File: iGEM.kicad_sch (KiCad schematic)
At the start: 50 parts, among them IC1 TMCS1107A1BQDRQ1, IC2 TMCS1107A1BQDRQ1, IC3 MCP4642-502E_UN, J1 Conn_01x02, J2 Conn_01x02, J3 Conn_01x02, J4 Conn_01x03, M1 Fan, Q1 TIP122, Q2 TIP122, Q3 IRF4905, Q4 D44VH, Q5 IRF4905, Q6 D44VH, U1 ADC101C021CIMK, U2 ADC101C021CIMK, U3 PCA9536D, U4 ICL7667

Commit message: updated mounting holes to M3
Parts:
- H1, H2, H3, H4: footprint MountingHole:MountingHole_5.3mm_M5_DIN965_Pad -> MountingHole:MountingHole_3.2mm_M3_DIN965_Pad
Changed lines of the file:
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@@
       (effects (font (size 1.27 1.27)) (justify left))
     )
-    (property "Footprint" "MountingHole:MountingHole_5.3mm_M5_DIN965_Pad" (id 2) (at 243.84 22.225 0)
+    (property "Footprint" "MountingHole:MountingHole_3.2mm_M3_DIN965_Pad" (id 2) (at 243.84 22.225 0)
       (effects (font (size 1.27 1.27)) hide)
     )
@@
       (effects (font (size 1.27 1.27)) (justify left))
     )
-    (property "Footprint" "MountingHole:MountingHole_5.3mm_M5_DIN965_Pad" (id 2) (at 228.727 22.098 0)
+    (property "Footprint" "MountingHole:MountingHole_3.2mm_M3_DIN965_Pad" (id 2) (at 228.727 22.098 0)
       (effects (font (size 1.27 1.27)) hide)
     )
@@
       (effects (font (size 1.27 1.27)) (justify left))
     )
-    (property "Footprint" "MountingHole:MountingHole_5.3mm_M5_DIN965_Pad" (id 2) (at 236.093 22.098 0)
+    (property "Footprint" "MountingHole:MountingHole_3.2mm_M3_DIN965_Pad" (id 2) (at 236.093 22.098 0)
       (effects (font (size 1.27 1.27)) hide)
     )
@@
       (effects (font (size 1.27 1.27)) (justify left))
     )
-    (property "Footprint" "MountingHole:MountingHole_5.3mm_M5_DIN965_Pad" (id 2) (at 220.98 21.971 0)
+    (property "Footprint" "MountingHole:MountingHole_3.2mm_M3_DIN965_Pad" (id 2) (at 220.98 21.971 0)
       (effects (font (size 1.27 1.27)) hide)
     )
@@
     )
     (path "/d8a1e4a6-2d49-424a-897c-8468ef6206d3"
-      (reference "H1") (unit 1) (value "MH") (footprint "MountingHole:MountingHole_5.3mm_M5_DIN965_Pad")
+      (reference "H1") (unit 1) (value "MH") (footprint "MountingHole:MountingHole_3.2mm_M3_DIN965_Pad")
     )
     (path "/a74e7590-46b6-4ec0-8175-bac4032efc02"
-      (reference "H2") (unit 1) (value "MH") (footprint "MountingHole:MountingHole_5.3mm_M5_DIN965_Pad")
+      (reference "H2") (unit 1) (value "MH") (footprint "MountingHole:MountingHole_3.2mm_M3_DIN965_Pad")
     )
     (path "/d1b51eea-8e22-4d48-82b7-9ab39c45531f"
-      (reference "H3") (unit 1) (value "MH") (footprint "MountingHole:MountingHole_5.3mm_M5_DIN965_Pad")
+      (reference "H3") (unit 1) (value "MH") (footprint "MountingHole:MountingHole_3.2mm_M3_DIN965_Pad")
     )
     (path "/7d301b82-72a3-482a-8606-544009d9efa6"
-      (reference "H4") (unit 1) (value "MH") (footprint "MountingHole:MountingHole_5.3mm_M5_DIN965_Pad")
+      (reference "H4") (unit 1) (value "MH") (footprint "MountingHole:MountingHole_3.2mm_M3_DIN965_Pad")
     )
     (path "/51879485-f54c-4d64-8de1-5fd9b52a4051"

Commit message: increased current capacity and added useful silk
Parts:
- J4: footprint Connector_JST:JST_XH_B3B-XH-AM_1x03_P2.50mm_Vertical -> Connector_JST:JST_XH_B3B-XH-A_1x03_P2.50mm_Vertical
- M1: footprint Connector_JST:JST_XH_B2B-XH-AM_1x02_P2.50mm_Vertical -> Connector_JST:JST_XH_B2B-XH-A_1x02_P2.50mm_Vertical
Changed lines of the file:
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@@
       (effects (font (size 1.27 1.27)) (justify left))
     )
-    (property "Footprint" "Connector_JST:JST_XH_B3B-XH-AM_1x03_P2.50mm_Vertical" (id 2) (at 226.695 58.039 0)
+    (property "Footprint" "Connector_JST:JST_XH_B3B-XH-A_1x03_P2.50mm_Vertical" (id 2) (at 226.695 58.039 0)
       (effects (font (size 1.27 1.27)) hide)
     )
@@
       (effects (font (size 1.27 1.27)) (justify left))
     )
-    (property "Footprint" "Connector_JST:JST_XH_B2B-XH-AM_1x02_P2.50mm_Vertical" (id 2) (at 263.398 26.924 0)
+    (property "Footprint" "Connector_JST:JST_XH_B2B-XH-A_1x02_P2.50mm_Vertical" (id 2) (at 263.398 26.924 0)
       (effects (font (size 1.27 1.27)) hide)
     )
@@
     )
     (path "/c0df6d10-baa8-43f2-8eaf-37632beb3c98"
-      (reference "J4") (unit 1) (value "Conn_01x03") (footprint "Connector_JST:JST_XH_B3B-XH-AM_1x03_P2.50mm_Vertical")
+      (reference "J4") (unit 1) (value "Conn_01x03") (footprint "Connector_JST:JST_XH_B3B-XH-A_1x03_P2.50mm_Vertical")
     )
     (path "/d65d8be2-cc90-4c64-af7a-fe7ceb3f9386"
-      (reference "M1") (unit 1) (value "Fan") (footprint "Connector_JST:JST_XH_B2B-XH-AM_1x02_P2.50mm_Vertical")
+      (reference "M1") (unit 1) (value "Fan") (footprint "Connector_JST:JST_XH_B2B-XH-A_1x02_P2.50mm_Vertical")
     )
     (path "/4b59aaf5-2612-4b64-b615-ddf78dad43ca"

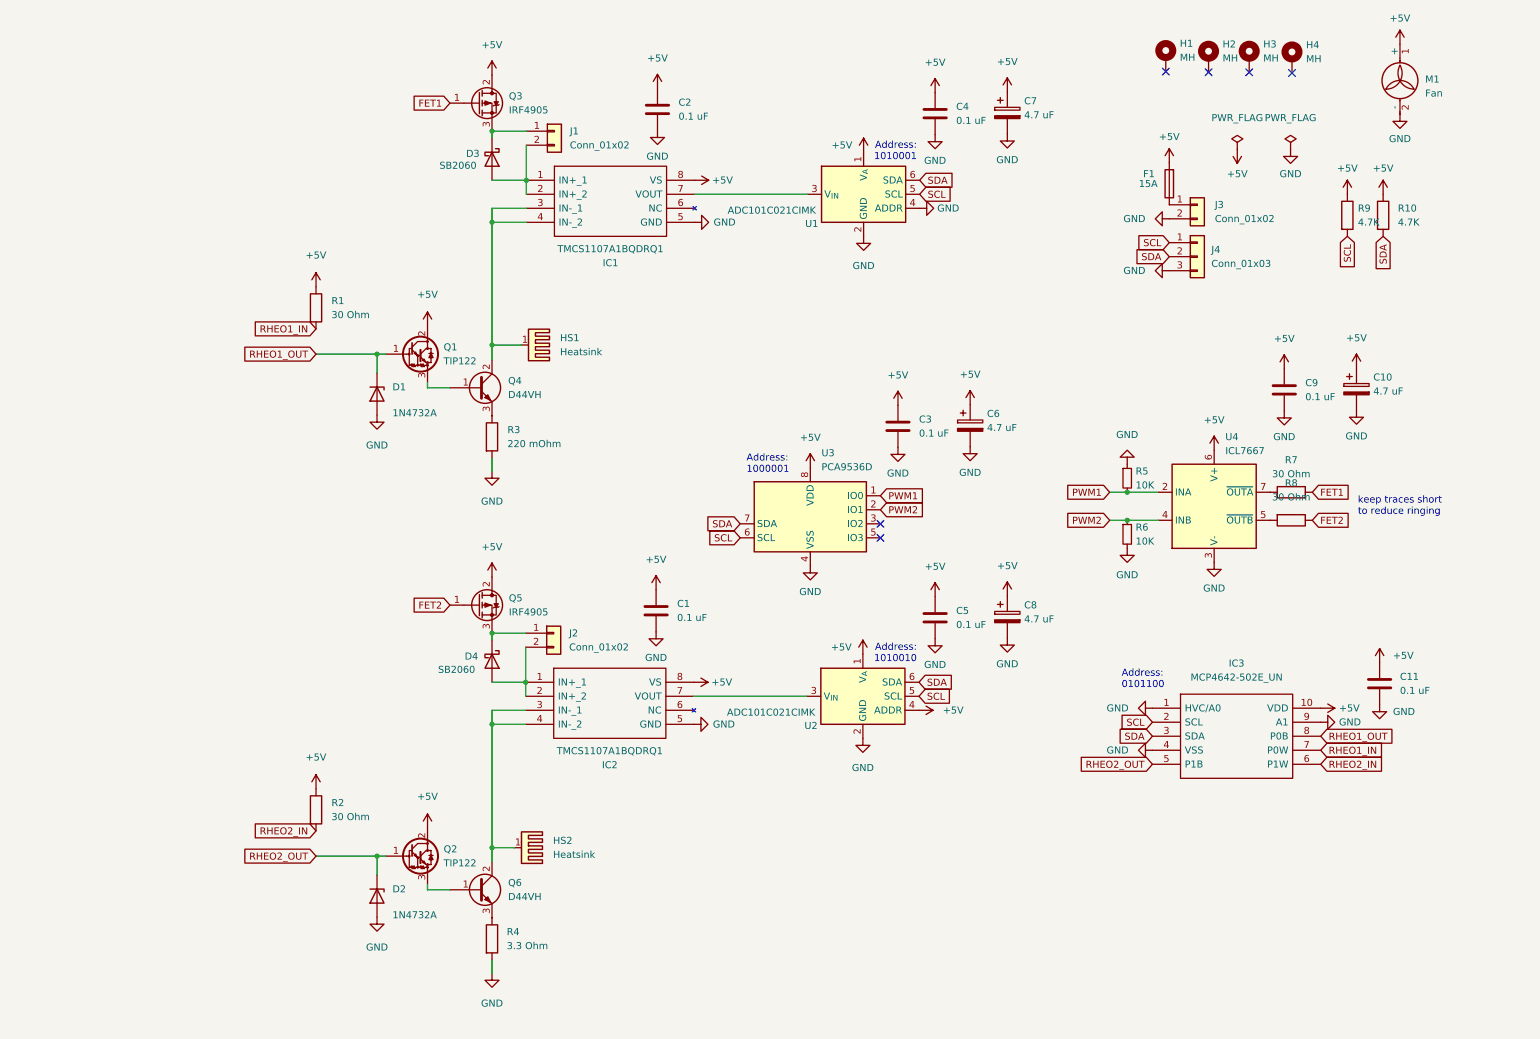
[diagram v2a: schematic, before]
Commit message: Changed to a single H-bridge for a single coil. Many parts changes. Addresses now configurable via pin header
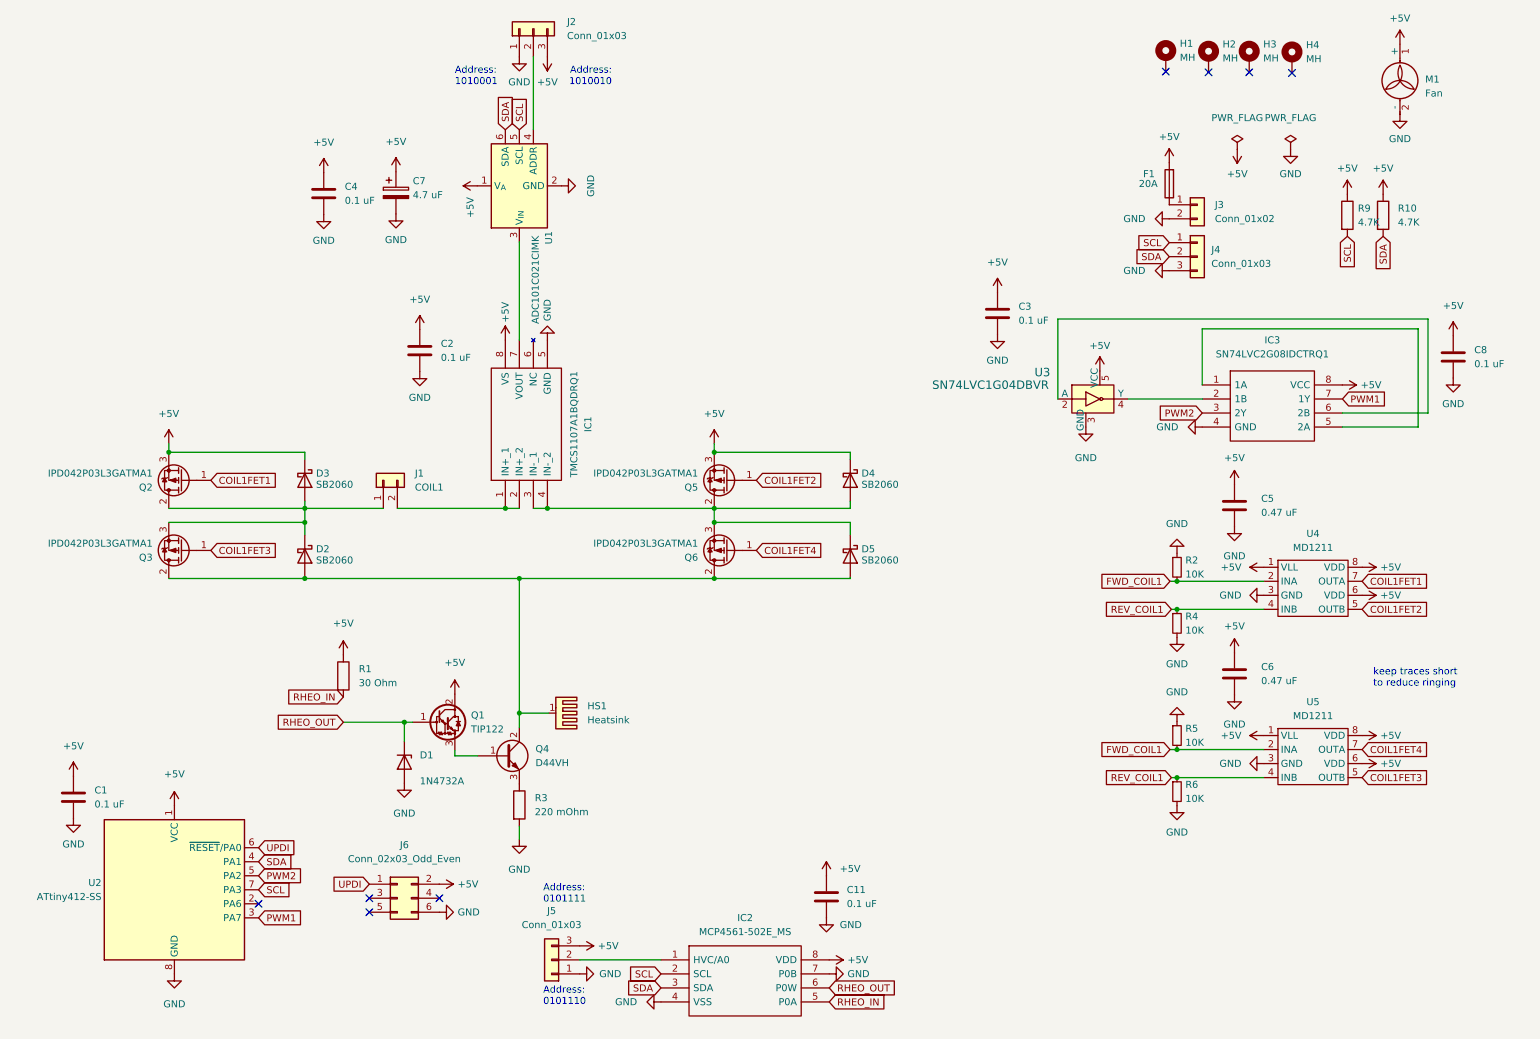
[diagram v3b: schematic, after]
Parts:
- removed C10, C6, C8: 4.7 uF, Capacitor_Tantalum_SMD:CP_EIA-3528-21_Kemet-B_Pad1.50x2.35mm_HandSolder, symbol Device:C_Polarized
- removed C9: 0.1 uF, Capacitor_SMD:C_0805_2012Metric_Pad1.18x1.45mm_HandSolder, symbol Device:C
- removed D2: 1N4732A, Diode_THT:D_DO-41_SOD81_P10.16mm_Horizontal, symbol Diode:1N47xxA
- removed HS2: Heatsink, Heatsink:Heatsink_AAVID_576802B03900G, symbol Mechanical:Heatsink_Pad
- removed IC2: TMCS1107A1BQDRQ1, Package_SO:SOIC-8_3.9x4.9mm_P1.27mm, symbol TMCS1107A1BQDRQ1:TMCS1107A1BQDRQ1
- removed IC3: MCP4642-502E_UN, Package_SO:MSOP-10_3x3mm_P0.5mm, symbol MCP4642-502E_UN:MCP4642-502E_UN
- removed J2: Conn_01x02, TerminalBlock:TerminalBlock_bornier-2_P5.08mm, symbol Connector_Generic:Conn_01x02
- removed Q2: TIP122, Package_TO_SOT_THT:TO-220-3_Vertical, symbol Transistor_BJT:TIP122
- removed Q3, Q5: IRF4905, Package_TO_SOT_THT:TO-220-3_Vertical, symbol Transistor_FET:IRF4905
- removed Q6: D44VH, Package_TO_SOT_THT:TO-220-3_Vertical, symbol Device:Q_NPN_BCE
- removed R2, R7, R8: 30 Ohm, Capacitor_SMD:C_0805_2012Metric_Pad1.18x1.45mm_HandSolder, symbol Device:R
- removed R4: 3.3 Ohm, TerminalBlock:TerminalBlock_bornier-2_P5.08mm, symbol Device:R
- removed U2: ADC101C021CIMK, Package_TO_SOT_SMD:SOT-23-6, symbol Analog_ADC:ADC101C021CIMK
- removed U3: PCA9536D, Package_SO:SOIC-8_3.9x4.9mm_P1.27mm, symbol Interface_Expansion:PCA9536D
- removed U4: ICL7667, Package_SO:SOIC-8_3.9x4.9mm_P1.27mm, symbol Driver_FET:ICL7667
- added C6: 0.47 uF, Capacitor_SMD:C_0805_2012Metric_Pad1.18x1.45mm_HandSolder, symbol Device:C
- added C8: 0.1 uF, Capacitor_SMD:C_0805_2012Metric_Pad1.18x1.45mm_HandSolder, symbol Device:C
- added D2, D5: SB2060, Diode_THT:D_DO-201AD_P12.70mm_Horizontal, symbol Device:D_Schottky
- added IC2: MCP4561-502E_MS, Package_SO:MSOP-8_3x3mm_P0.65mm, symbol MCP4561-502E_MS:MCP4561-502E_MS
- added IC3: SN74LVC2G08IDCTRQ1, Package_SO:MSOP-8_3x3mm_P0.65mm, symbol SN74LVC2G08IDCTRQ1:SN74LVC2G08IDCTRQ1
- added J2, J5: Conn_01x03, Connector_PinHeader_2.54mm:PinHeader_1x03_P2.54mm_Vertical, symbol Connector_Generic:Conn_01x03
- added J6: Conn_02x03_Odd_Even, Connector_PinHeader_2.54mm:PinHeader_2x03_P2.54mm_Vertical, symbol Connector_Generic:Conn_02x03_Odd_Even
- added Q2, Q3, Q5, Q6: IPD042P03L3GATMA1, Package_TO_SOT_SMD:TO-252-2, symbol Device:Q_PMOS_GDS
- added R2, R4: 10K, Capacitor_SMD:C_0805_2012Metric_Pad1.18x1.45mm_HandSolder, symbol Device:R_Small
- added U2: ATtiny412-SS, Package_SO:SOIC-8_3.9x4.9mm_P1.27mm, symbol MCU_Microchip_ATtiny:ATtiny412-SS
- added U3: SN74LVC1G04DBVR, digikey-footprints:SOT-753, symbol dk_Logic-Gates-and-Inverters:SN74LVC1G04DBVR
- added U4, U5: MD1211, Package_SO:SOIC-8_3.9x4.9mm_P1.27mm, symbol MD1211:MD1211
- C5: value 0.1 uF -> 0.47 uF; DigiKey 399-C0805C104K8RAC7800CT-ND -> 399-C0805C474K8RAC7800CT-ND
- F1: value 15A -> 20A
- J1: value Conn_01x02 -> COIL1
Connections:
- net +5V: now also D3.1 (K), D4.1 (K), C6.1, C8.1, IC2.8 (VDD), IC3.8 (VCC), J2.3 (Pin_3), J5.3 (Pin_3), J6.2 (Pin_2), Q2.3 (S), Q5.3 (S), U2.1 (VCC), U3.5 (VCC), U4.1 (VLL), U4.6 (VDD), U4.8 (VDD), U5.1 (VLL), U5.6 (VDD), U5.8 (VDD)
- net GND: now also C6.2, C8.2, IC2.4 (VSS), IC2.7 (P0B), IC3.4 (GND), J2.1 (Pin_1), J5.1 (Pin_1), J6.6 (Pin_6), R2.1, R4.2, U2.8 (GND), U3.3 (GND), U4.3 (GND), U5.3 (GND); no longer U1.4 (ADDR)
- net PWM1: now also IC3.7 (1Y), U2.3 (PA7); no longer R5.2
- net PWM2: now also IC3.3 (2Y), U2.5 (PA2); no longer R6.1
- net SCL: now also IC2.2 (SCL), U2.7 (PA3)
- net SDA: now also IC2.3 (SDA), U2.4 (PA1)
- net at J1.1 (Pin_1): now also D3.2 (A), D2.1 (K), Q2.2 (D), Q3.3 (S); no longer D3.1 (K)
- net at IC1.1 (IN+_1), IC1.2 (IN+_2), J1.2 (Pin_2): no longer D3.2 (A)
- net at HS1.1, Q4.2 (C): now also D2.2 (A), D5.2 (A), Q3.2 (D), Q6.2 (D); no longer IC1.3 (IN-_1), IC1.4 (IN-_2)
- net at D4.2 (A): now also IC1.3 (IN-_1), IC1.4 (IN-_2), D5.1 (K), Q5.2 (D), Q6.3 (S)
- net RHEO1_IN renamed RHEO_IN
- net RHEO_IN: now also IC2.5 (P0A)
- net RHEO1_OUT renamed RHEO_OUT
- net RHEO_OUT: now also IC2.6 (P0W)
- new net: IC2.1 (HVC/A0), J5.2 (Pin_2)
- new net: J2.2 (Pin_2), U1.4 (ADDR)
- new net: IC3.6 (2B), U3.2 (A)
- new net: IC3.2 (1B), U3.4 (Y)
- new net: IC3.1 (1A), IC3.5 (2A)
- new net COIL1FET1: Q2.1 (G), U4.7 (OUTA)
- new net COIL1FET2: Q5.1 (G), U4.5 (OUTB)
- new net COIL1FET3: Q3.1 (G), U5.5 (OUTB)
- new net COIL1FET4: Q6.1 (G), U5.7 (OUTA)
- new net FWD_COIL1: R2.2, R5.2, U4.2 (INA), U5.2 (INA)
- new net REV_COIL1: R4.1, R6.1, U4.4 (INB), U5.4 (INB)
- new net UPDI: J6.1 (Pin_1), U2.6 (~{RESET}/PA0)
- no-connect marks 6 -> 8
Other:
- note added: "Address: 0101110"
- note added: "Address: 0101111"
- note removed: "Address: 0101100"
- note removed: "Address: 1000001"
- moved on the sheet: C11, C2, C4, C7, D1, D3, HS1, IC1, J1, Q1, Q4, R1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
